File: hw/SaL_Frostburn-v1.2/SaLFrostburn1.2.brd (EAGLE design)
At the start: 72.7 x 19.8 mm, 99 parts, among them U1 ATSAMD21G-A, U3 ADXL345, U4 gps, Y1 32.768kHx, Y3 32MHz

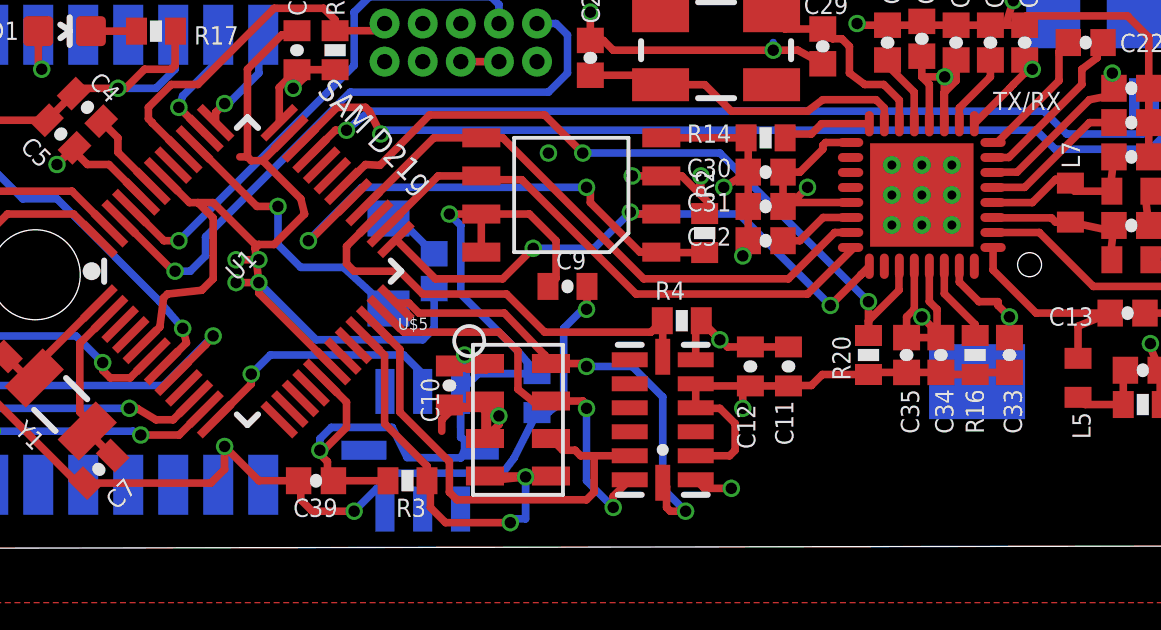
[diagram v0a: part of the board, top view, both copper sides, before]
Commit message: added buzzer to 1.2 hw and setup 1.1 in studio
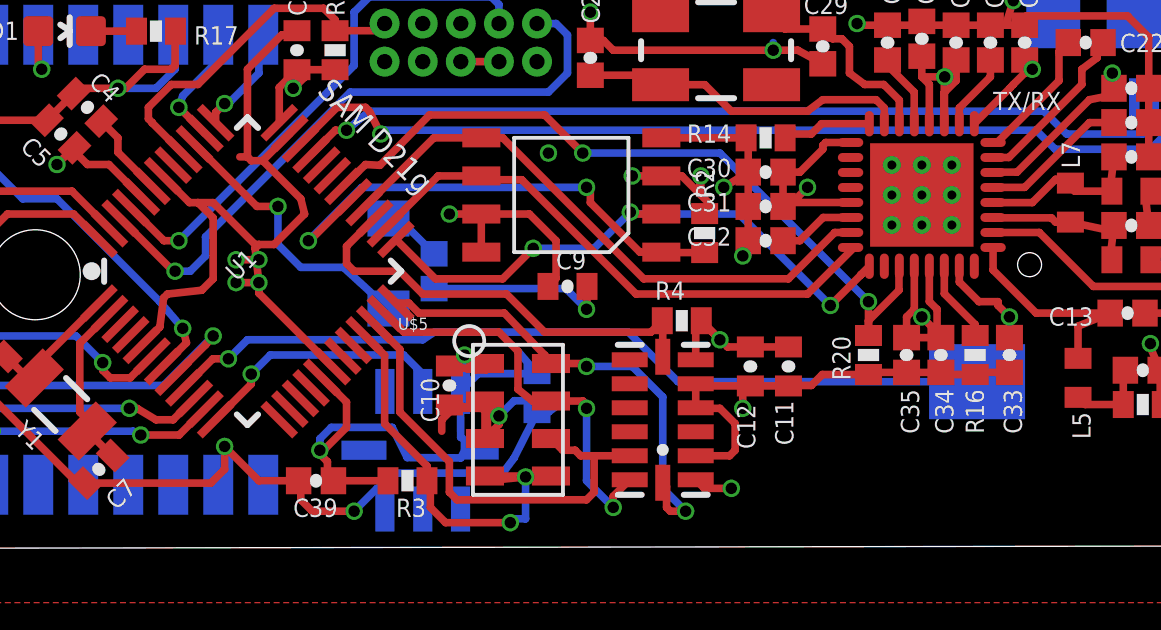
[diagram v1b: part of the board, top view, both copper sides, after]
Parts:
- JP5: value (none) -> Lipo
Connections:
- net BUZZER: now also U1.9
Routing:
- net BUZZER: track 0.00 -> 27.9 mm, vias 0 -> 1
- net GND: track 356.8 -> 358.6 mm
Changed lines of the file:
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@@
 <element name="U$4" library="SaL-lib1" package="POWERPACK1212-8" value="SIS410DN" x="8.763" y="11.303" rot="R90"/>
 <element name="U$6" library="SaL-lib1" package="POWERPACK1212-8" value="SIS410DN" x="10.795" y="8.255" rot="R270"/>
-<element name="JP5" library="SparkFun-Connectors" package="JST-2-SMD-VERT" value="" x="-0.635" y="9.779" rot="MR270"/>
+<element name="JP5" library="SparkFun-Connectors" package="JST-2-SMD-VERT" value="Lipo" x="-0.635" y="9.779" rot="MR270"/>
 <element name="STANDOFF4" library="SparkFun-Electromechanical" package="STAND-OFF" value="STAND-OFF" x="65.278" y="2.667"/>
 <element name="U$7" library="SparkFun-Sensors" package="ADXL193" value="ADXL193" x="31.75" y="3.175" smashed="yes" rot="MR90">
@@
 <wire x1="35.306" y1="14.732" x2="35.687" y2="15.113" width="0.254" layer="15"/>
 <wire x1="35.56" y1="5.73" x2="34.925" y2="6.477" width="0.254" layer="16"/>
-<wire x1="34.925" y1="6.477" x2="33.02" y2="8.382" width="0.254" layer="16"/>
-<wire x1="33.02" y1="8.382" x2="33.02" y2="10.668" width="0.254" layer="16"/>
-<wire x1="33.02" y1="10.668" x2="32.639" y2="11.049" width="0.254" layer="16"/>
 <wire x1="33.87" y1="5.857" x2="33.513" y2="5.857" width="0.254" layer="1"/>
 <wire x1="33.513" y1="5.857" x2="33.147" y2="6.35" width="0.254" layer="1"/>
@@
 <wire x1="51.816" y1="15.748" x2="52.07" y2="15.875" width="0.254" layer="1"/>
 <wire x1="52.07" y1="15.875" x2="52.07" y2="15.621" width="0.254" layer="15"/>
+<wire x1="32.639" y1="11.049" x2="33.147" y2="11.049" width="0.4064" layer="15"/>
+<wire x1="33.147" y1="11.049" x2="33.147" y2="6.35" width="0.4064" layer="15"/>
 </signal>
 <signal name="GND">
@@
 <wire x1="27.813" y1="11.049" x2="27.686" y2="11.557" width="0.254" layer="1"/>
 <wire x1="27.686" y1="11.557" x2="26.416" y2="12.827" width="0.254" layer="1"/>
-<wire x1="32.131" y1="8.564" x2="32.131" y2="7.239" width="0.254" layer="16"/>
-<wire x1="32.131" y1="7.239" x2="31.75" y2="6.858" width="0.254" layer="16"/>
-<wire x1="31.75" y1="6.858" x2="28.194" y2="6.858" width="0.254" layer="16"/>
-<wire x1="28.194" y1="6.858" x2="26.289" y2="8.763" width="0.254" layer="16"/>
 <via x="26.289" y="8.763" extent="1-16" drill="0.381"/>
 <wire x1="26.289" y1="8.763" x2="26.20226875" y2="9.543584375" width="0.254" layer="1"/>
@@
 <wire x1="35.575" y1="4.445" x2="35.941" y2="4.445" width="0.254" layer="16"/>
 <wire x1="35.941" y1="4.445" x2="36.449" y2="4.826" width="0.254" layer="16"/>
-<wire x1="36.449" y1="4.826" x2="36.449" y2="7.239" width="0.254" layer="16"/>
-<wire x1="36.449" y1="7.239" x2="37.084" y2="7.874" width="0.254" layer="16"/>
-<wire x1="37.084" y1="7.874" x2="37.211" y2="7.874" width="0.254" layer="16"/>
 <wire x1="29.464" y1="1.143" x2="29.464" y2="3.81" width="0.254" layer="2"/>
 <wire x1="29.464" y1="3.81" x2="29.464" y2="5.588" width="0.254" layer="2"/>
@@
 <wire x1="11.034" y1="9.652" x2="10.668" y2="10.414" width="0.254" layer="16"/>
 <wire x1="35.941" y1="13.081" x2="34.29" y2="16.129" width="0.254" layer="2"/>
+<wire x1="36.449" y1="4.826" x2="34.798" y2="4.826" width="0.254" layer="16"/>
+<wire x1="34.798" y1="4.826" x2="34.29" y2="4.318" width="0.254" layer="16"/>
+<wire x1="37.211" y1="7.874" x2="35.687" y2="7.874" width="0.254" layer="2"/>
+<wire x1="35.687" y1="7.874" x2="34.29" y2="6.477" width="0.254" layer="2"/>
+<wire x1="34.29" y1="6.477" x2="34.29" y2="4.318" width="0.254" layer="2"/>
+<wire x1="32.131" y1="8.564" x2="36.521" y2="8.564" width="0.254" layer="16"/>
+<wire x1="36.521" y1="8.564" x2="37.211" y2="7.874" width="0.254" layer="16"/>
 </signal>
 <signal name="LVD_IN">
@@
 <signal name="BUZZER">
 <contactref element="SG1" pad="+"/>
+<contactref element="U1" pad="9"/>
+<wire x1="50.229" y1="5.461" x2="40.259" y2="5.461" width="0.254" layer="16"/>
+<wire x1="40.259" y1="5.461" x2="38.608" y2="7.112" width="0.254" layer="16"/>
+<wire x1="38.608" y1="7.112" x2="32.131" y2="7.112" width="0.254" layer="16"/>
+<wire x1="32.131" y1="7.112" x2="31.75" y2="6.858" width="0.254" layer="16"/>
+<wire x1="31.75" y1="6.858" x2="25.908" y2="6.858" width="0.254" layer="16"/>
+<wire x1="25.908" y1="6.858" x2="25.273" y2="6.223" width="0.254" layer="16"/>
+<via x="25.273" y="6.223" extent="1-16" drill="0.381"/>
+<wire x1="25.273" y1="6.223" x2="24.754765625" y2="6.223" width="0.254" layer="1"/>
+<wire x1="24.754765625" y1="6.223" x2="23.786678125" y2="5.2549125" width="0.254" layer="1"/>
 </signal>
 <signal name="N$7">

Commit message: 1.2 hw sent to fab and some work on 1.1 code
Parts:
- removed FRAME1: FRAME-LEDGER, SparkFun-Aesthetics:CREATIVE_COMMONS
- moved C12 4.70 mm to (47.4, 6.10)
- moved C13 4.70 mm to (59.9, 7.87)
- moved C35 4.70 mm to (52.6, 6.48)
- moved JP4 4.70 mm to (61.5, 17.7)
- moved L4 4.70 mm to (66.9, 10.2)
- moved L6 4.70 mm to (63.2, 11.9)
- moved U$5 4.70 mm to (39.6, 4.32)
- moved U3 4.70 mm to (44.5, 4.32)
- moved C39 4.70 mm to (32.9, 2.29)
- moved C5 4.70 mm to (24.4, 13.8)
- moved C7 4.70 mm to (25.7, 2.67)
- moved C8 4.70 mm to (32.3, 16.6)
- moved L1 4.70 mm to (19.4, 9.78)
- moved R17 4.70 mm to (27.6, 17.3)
- moved R3 4.70 mm to (35.9, 2.29)
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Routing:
- net GND: track 358.6 -> 362.1 mm
- net N$13: vias 0 -> 1
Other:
- outline, holes or cut-outs redrawn
- board text added: "SaLFrostburn V1.2"
- board text removed: "SaLFrostburn V1.1"

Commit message: not real changes
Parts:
- added STANDOFF5: STAND-OFF, SparkFun-Electromechanical:STAND-OFF
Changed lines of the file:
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@@
 <?xml version="1.0" encoding="utf-8"?>
 <!DOCTYPE eagle SYSTEM "eagle.dtd">
-<eagle version="7.5.0">
+<eagle version="8.3.1">
 <drawing>
 <settings>
 <setting alwaysvectorfont="no"/>
+<setting keepoldvectorfont="yes"/>
 <setting verticaltext="up"/>
 </settings>
@@
 <elements>
 <element name="U1" library="SparkFun-DigitalIC" package="TQFP-48" value="ATSAMD21G-A" x="30.607" y="9.271" smashed="yes" rot="R45">
+<attribute name="NAME" x="30.607" y="9.271" size="0.6096" layer="25" rot="R45" align="bottom-center"/>
 <attribute name="PROD_ID" value="IC-13064" x="30.607" y="9.271" size="1.778" layer="27" rot="R45" display="off"/>
-<attribute name="NAME" x="30.607" y="9.271" size="0.6096" layer="25" rot="R45" align="bottom-center"/>
 <attribute name="VALUE" x="31.505025" y="8.372971875" size="0.8128" layer="27" rot="R45" align="bottom-center"/>
 </element>
@@
 </element>
 <element name="Y3" library="SparkFun-FreqCtrl" package="CRYSTAL-SMD-5X3" value="32MHz" x="46.228" y="16.637" smashed="yes">
+<attribute name="NAME" x="45.593" y="18.542" size="0.6096" layer="25"/>
 <attribute name="PROD_ID" value="XTAL-08218" x="46.228" y="16.637" size="1.778" layer="27" display="off"/>
-<attribute name="NAME" x="45.593" y="18.542" size="0.6096" layer="25"/>
 </element>
 <element name="R14" library="SparkFun-Passives" package="0402-RES" value="0ohm" x="47.879" y="13.716" smashed="yes" rot="R180">
@@
 <element name="U4" library="adafruit" package="FGPMMOPA6H" value="gps" x="24.384" y="9.652" rot="MR270"/>
 <element name="D1" library="SparkFun-LED" package="LED-0603" value="RED" x="24.511" y="17.272" smashed="yes" rot="R270">
+<attribute name="NAME" x="22.987" y="17.5895" size="0.6096" layer="25" rot="R180"/>
 <attribute name="PROD_ID" value="DIO-00819" x="24.511" y="17.272" size="1.778" layer="27" rot="R270" display="off"/>
-<attribute name="NAME" x="22.987" y="17.5895" size="0.6096" layer="25" rot="R180"/>
 </element>
 <element name="R17" library="SparkFun-Passives" package="0402-RES" value="301ohm\" x="27.559" y="17.272" smashed="yes" rot="R180">
@@
 </element>
 <element name="S2" library="SparkFun-Electromechanical" package="TACTILE_SWITCH_SMD_4.6X2.8MM" value="SWITCH-MOMENTARY-2SMD-4.6X2.8MM" x="8.128" y="3.937" smashed="yes" rot="MR270">
+<attribute name="NAME" x="6.604" y="6.477" size="0.8128" layer="26" rot="MR270"/>
 <attribute name="PROD_ID" value="SWCH-13065" x="8.128" y="3.937" size="1.778" layer="28" rot="MR270" display="off"/>
-<attribute name="NAME" x="6.604" y="6.477" size="0.8128" layer="26" rot="MR270"/>
 </element>
 <element name="STANDOFF1" library="SparkFun-Electromechanical" package="STAND-OFF" value="STAND-OFF" x="69.977" y="17.018"/>
@@
 </element>
 <element name="D2" library="SparkFun-LED" package="LED-1206" value="GREEN" x="35.306" y="9.525" smashed="yes" rot="MR90">
+<attribute name="NAME" x="33.909" y="9.017" size="0.6096" layer="26" rot="MR90"/>
 <attribute name="PROD_ID" value="DIO-00862" x="35.306" y="9.525" size="1.778" layer="28" rot="MR90" display="off"/>
-<attribute name="NAME" x="33.909" y="9.017" size="0.6096" layer="26" rot="MR90"/>
 </element>
 <element name="R21" library="SparkFun-Resistors" package="0402-RES" value="63" x="36.83" y="9.271" smashed="yes" rot="MR270">
@@
 <attribute name="NAME" x="41.4655" y="6.096" size="0.6096" layer="26" rot="MR270"/>
 </element>
+<element name="STANDOFF5" library="SparkFun-Electromechanical" package="STAND-OFF" value="STAND-OFF" x="1.905" y="-6.985"/>
 </elements>
 <signals>
